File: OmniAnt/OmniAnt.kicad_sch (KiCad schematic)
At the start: 30 parts, among them J1 Conn_01x02_Pin, J2 Conn_01x01, J3 Connector, USB-TYPE-C-16P, J4 Conn_01x01, J5 Conn_01x01, J6 XT30PW-M, J7 XT30PW-M, J8 XT30PW-M, J9 XT30PW-M, U1 ESP32-S3-WROOM-1, U2 TPSM53603RDA, U4 USBLC6-2P6

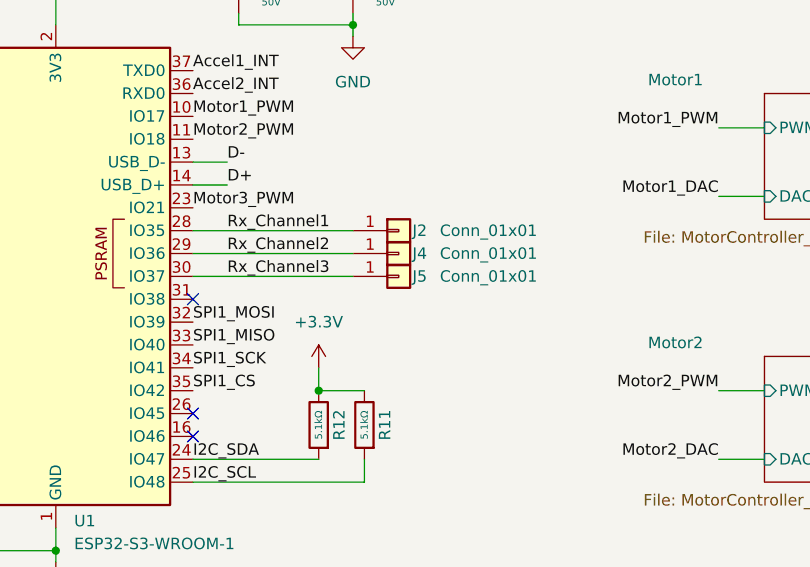
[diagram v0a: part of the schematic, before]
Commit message: added a link to the motor controller datasheet and changed the connector footprint for the RC interface.
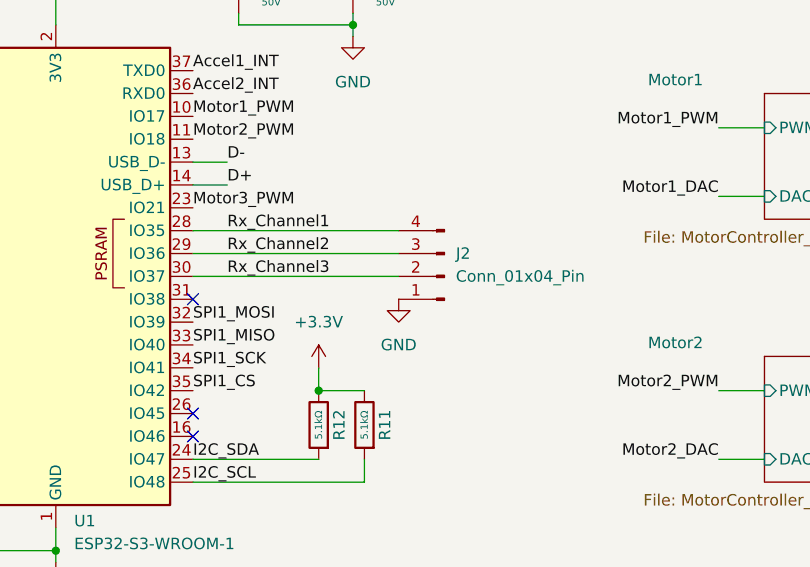
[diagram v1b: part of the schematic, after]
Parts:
- removed J2, J4, J5: Conn_01x01, symbol Connector_Generic:Conn_01x01
- added J2: Conn_01x04_Pin, Connector_PinHeader_2.54mm:PinHeader_1x04_P2.54mm_Vertical, symbol Connector:Conn_01x04_Pin
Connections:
- net GND: now also J2.1 (Pin_1)
- net Rx_Channel1: now also J2.4 (Pin_4)
- net Rx_Channel2: now also J2.3 (Pin_3)
- net Rx_Channel3: now also J2.2 (Pin_2)
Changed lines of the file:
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@@
 	(wire
 		(pts
-			(xy 171.45 127) (xy 189.23 127)
+			(xy 171.45 127) (xy 194.31 127)
 		)
 		(stroke
@@
 	(wire
 		(pts
-			(xy 171.45 124.46) (xy 189.23 124.46)
+			(xy 171.45 124.46) (xy 194.31 124.46)
 		)
 		(stroke
@@
 	(wire
 		(pts
-			(xy 171.45 121.92) (xy 189.23 121.92)
+			(xy 171.45 121.92) (xy 194.31 121.92)
 		)
 		(stroke
@@
 	)
 	(symbol
-		(lib_id "Connector_Generic:Conn_01x01")
-		(at 194.31 124.46 0)
-		(unit 1)
-		(exclude_from_sim no)
-		(in_bom yes)
-		(on_board yes)
-		(dnp no)
-		(property "Reference" "J4"
-			(at 195.834 124.4599 0)
-			(effects
-				(font
-					(size 1.27 1.27)
-				)
-				(justify left)
-			)
-		)
-		(property "Value" "Conn_01x01"
-			(at 198.882 124.46 0)
-			(effects
-				(font
-					(size 1.27 1.27)
-				)
-				(justify left)
-			)
-		)
-		(property "Footprint" ""
-			(at 194.31 124.46 0)
-			(effects
-				(font
-					(size 1.27 1.27)
-				)
-				(hide yes)
-			)
-		)
-		(property "Datasheet" "~"
-			(at 194.31 124.46 0)
-			(effects
-				(font
-					(size 1.27 1.27)
-				)
-				(hide yes)
-			)
-		)
-		(property "Description" "Generic connector, single row, 01x01, script generated (kicad-library-utils/schlib/autogen/connector/)"
-			(at 194.31 124.46 0)
-			(effects
-				(font
-					(size 1.27 1.27)
-				)
-				(hide yes)
-			)
-		)
-		(pin "1"
-		)
-		(instances
-			(project "OmniAnt"
-				(path "/af956454-8f11-4118-89f4-dd7ed925536a"
-					(reference "J4")
-					(unit 1)
-				)
-			)
-		)
-	)
-	(symbol
 		(lib_id "power:GND")
 		(at 115.57 114.3 0)
@@
 	)
 	(symbol
+		(lib_id "power:GND")
+		(at 194.31 129.54 0)
+		(unit 1)
+		(exclude_from_sim no)
+		(in_bom yes)
+		(on_board yes)
+		(dnp no)
+		(fields_autoplaced yes)
+		(property "Reference" "#PWR029"
+			(at 194.31 135.89 0)
+			(effects
+				(font
+					(size 1.27 1.27)
+				)
+				(hide yes)
+			)
+		)
+		(property "Value" "GND"
+			(at 194.31 134.62 0)
+			(effects
+				(font
+					(size 1.27 1.27)
+				)
+			)
+		)
+		(property "Footprint" ""
+			(at 194.31 129.54 0)
+			(effects
+				(font
+					(size 1.27 1.27)
+				)
+				(hide yes)
+			)
+		)
+		(property "Datasheet" ""
+			(at 194.31 129.54 0)
+			(effects
+				(font
+					(size 1.27 1.27)
+				)
+				(hide yes)
+			)
+		)
+		(property "Description" "Power symbol creates a global label with name \"GND\" , ground"
+			(at 194.31 129.54 0)
+			(effects
+				(font
+					(size 1.27 1.27)
+				)
+				(hide yes)
+			)
+		)
+		(pin "1"
+		)
+		(instances
+			(project "OmniAnt"
+				(path "/af956454-8f11-4118-89f4-dd7ed925536a"
+					(reference "#PWR029")
+					(unit 1)
+				)
+			)
+		)
+	)
+	(symbol
 		(lib_id "Power_Protection:USBLC6-2P6")
 		(at 76.2 40.64 0)
@@
 	)
 	(symbol
+		(lib_id "Connector:Conn_01x04_Pin")
+		(at 199.39 127 180)
+		(unit 1)
+		(exclude_from_sim no)
+		(in_bom yes)
+		(on_board yes)
+		(dnp no)
+		(fields_autoplaced yes)
+		(property "Reference" "J2"
+			(at 200.66 124.4599 0)
+			(effects
+				(font
+					(size 1.27 1.27)
+				)
+				(justify right)
+			)
+		)
+		(property "Value" "Conn_01x04_Pin"
+			(at 200.66 126.9999 0)
+			(effects
+				(font
+					(size 1.27 1.27)
+				)
+				(justify right)
+			)
+		)
+		(property "Footprint" "Connector_PinHeader_2.54mm:PinHeader_1x04_P2.54mm_Vertical"
+			(at 199.39 127 0)
+			(effects
+				(font
+					(size 1.27 1.27)
+				)
+				(hide yes)
+			)
+		)
+		(property "Datasheet" "~"
+			(at 199.39 127 0)
+			(effects
+				(font
+					(size 1.27 1.27)
+				)
+				(hide yes)
+			)
+		)
+		(property "Description" "Generic connector, single row, 01x04, script generated"
+			(at 199.39 127 0)
+			(effects
+				(font
+					(size 1.27 1.27)
+				)
+				(hide yes)
+			)
+		)
+		(pin "1"
+		)
+		(pin "3"
+		)
+		(pin "2"
+		)
+		(pin "4"
+		)
+		(instances
+			(project ""
+				(path "/af956454-8f11-4118-89f4-dd7ed925536a"
+					(reference "J2")
+					(unit 1)
+				)
+			)
+		)
+	)
+	(symbol
 		(lib_id "power:GND")
 		(at 62.23 30.48 0)
@@
 	)
 	(symbol
-		(lib_id "Connector_Generic:Conn_01x01")
-		(at 194.31 121.92 0)
-		(unit 1)
-		(exclude_from_sim no)
-		(in_bom yes)
-		(on_board yes)
-		(dnp no)
-		(property "Reference" "J2"
-			(at 195.834 121.9199 0)
-			(effects
-				(font
-					(size 1.27 1.27)
-				)
-				(justify left)
-			)
-		)
-		(property "Value" "Conn_01x01"
-			(at 198.882 121.92 0)
-			(effects
-				(font
-					(size 1.27 1.27)
-				)
-				(justify left)
-			)
-		)
-		(property "Footprint" ""
-			(at 194.31 121.92 0)
-			(effects
-				(font
-					(size 1.27 1.27)
-				)
-				(hide yes)
-			)
-		)
-		(property "Datasheet" "~"
-			(at 194.31 121.92 0)
-			(effects
-				(font
-					(size 1.27 1.27)
-				)
-				(hide yes)
-			)
-		)
-		(property "Description" "Generic connector, single row, 01x01, script generated (kicad-library-utils/schlib/autogen/connector/)"
-			(at 194.31 121.92 0)
-			(effects
-				(font
-					(size 1.27 1.27)
-				)
-				(hide yes)
-			)
-		)
-		(pin "1"
-		)
-		(instances
-			(project ""
-				(path "/af956454-8f11-4118-89f4-dd7ed925536a"
-					(reference "J2")
-					(unit 1)
-				)
-			)
-		)
-	)
-	(symbol
 		(lib_id "XT30PW-M:XT30PW-M")
 		(at 208.28 26.67 0)
@@
 					(unit 1)
 				)
-			)
-		)
-	)
-	(symbol
-		(lib_id "Connector_Generic:Conn_01x01")
-		(at 194.31 127 0)
-		(unit 1)
-		(exclude_from_sim no)
-		(in_bom yes)
-		(on_board yes)
-		(dnp no)
-		(property "Reference" "J5"
-			(at 195.834 126.9999 0)
-			(effects
-				(font
-					(size 1.27 1.27)
-				)
-				(justify left)
-			)
-		)
-		(property "Value" "Conn_01x01"
-			(at 198.882 127 0)
-			(effects
-				(font
-					(size 1.27 1.27)
-				)
-				(justify left)
-			)
-		)
-		(property "Footprint" ""
-			(at 194.31 127 0)
-			(effects
-				(font
-					(size 1.27 1.27)
-				)
-				(hide yes)
-			)
-		)
-		(property "Datasheet" "~"
-			(at 194.31 127 0)
-			(effects
-				(font
-					(size 1.27 1.27)
-				)
-				(hide yes)
-			)
-		)
-		(property "Description" "Generic connector, single row, 01x01, script generated (kicad-library-utils/schlib/autogen/connector/)"
-			(at 194.31 127 0)
-			(effects
-				(font
-					(size 1.27 1.27)
-				)
-				(hide yes)
-			)
-		)
-		(pin "1"
-		)
-		(instances
-			(project "OmniAnt"
-				(path "/af956454-8f11-4118-89f4-dd7ed925536a"
-					(reference "J5")
-					(unit 1)
-				)

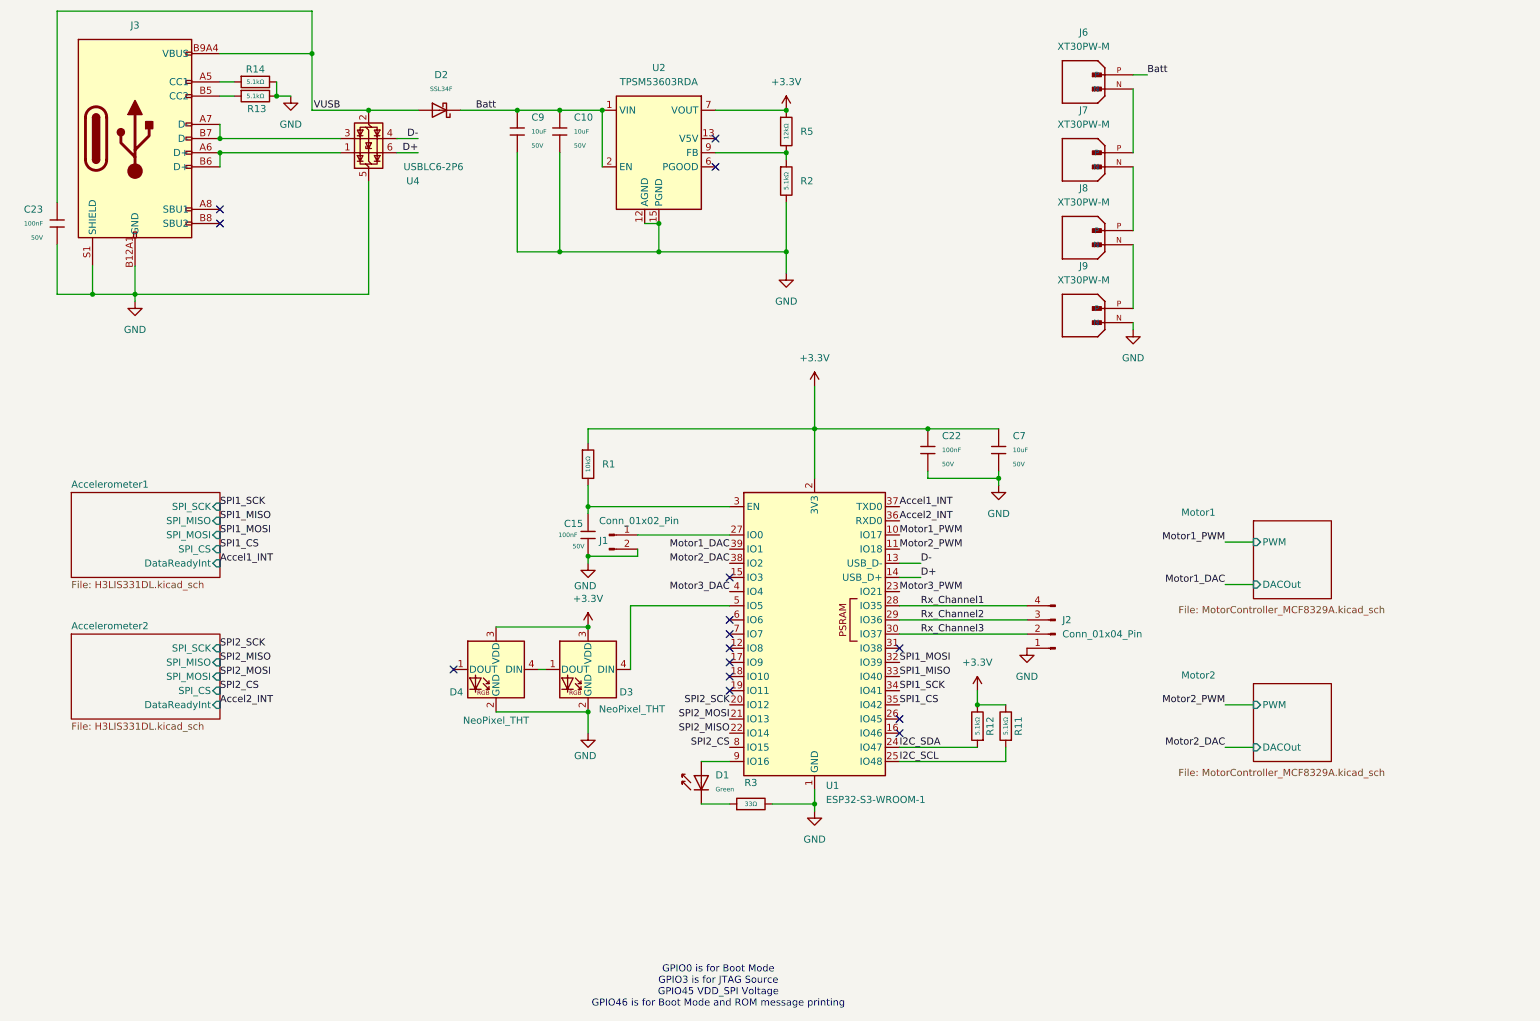
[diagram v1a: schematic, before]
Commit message: fixed all the schematic errors.
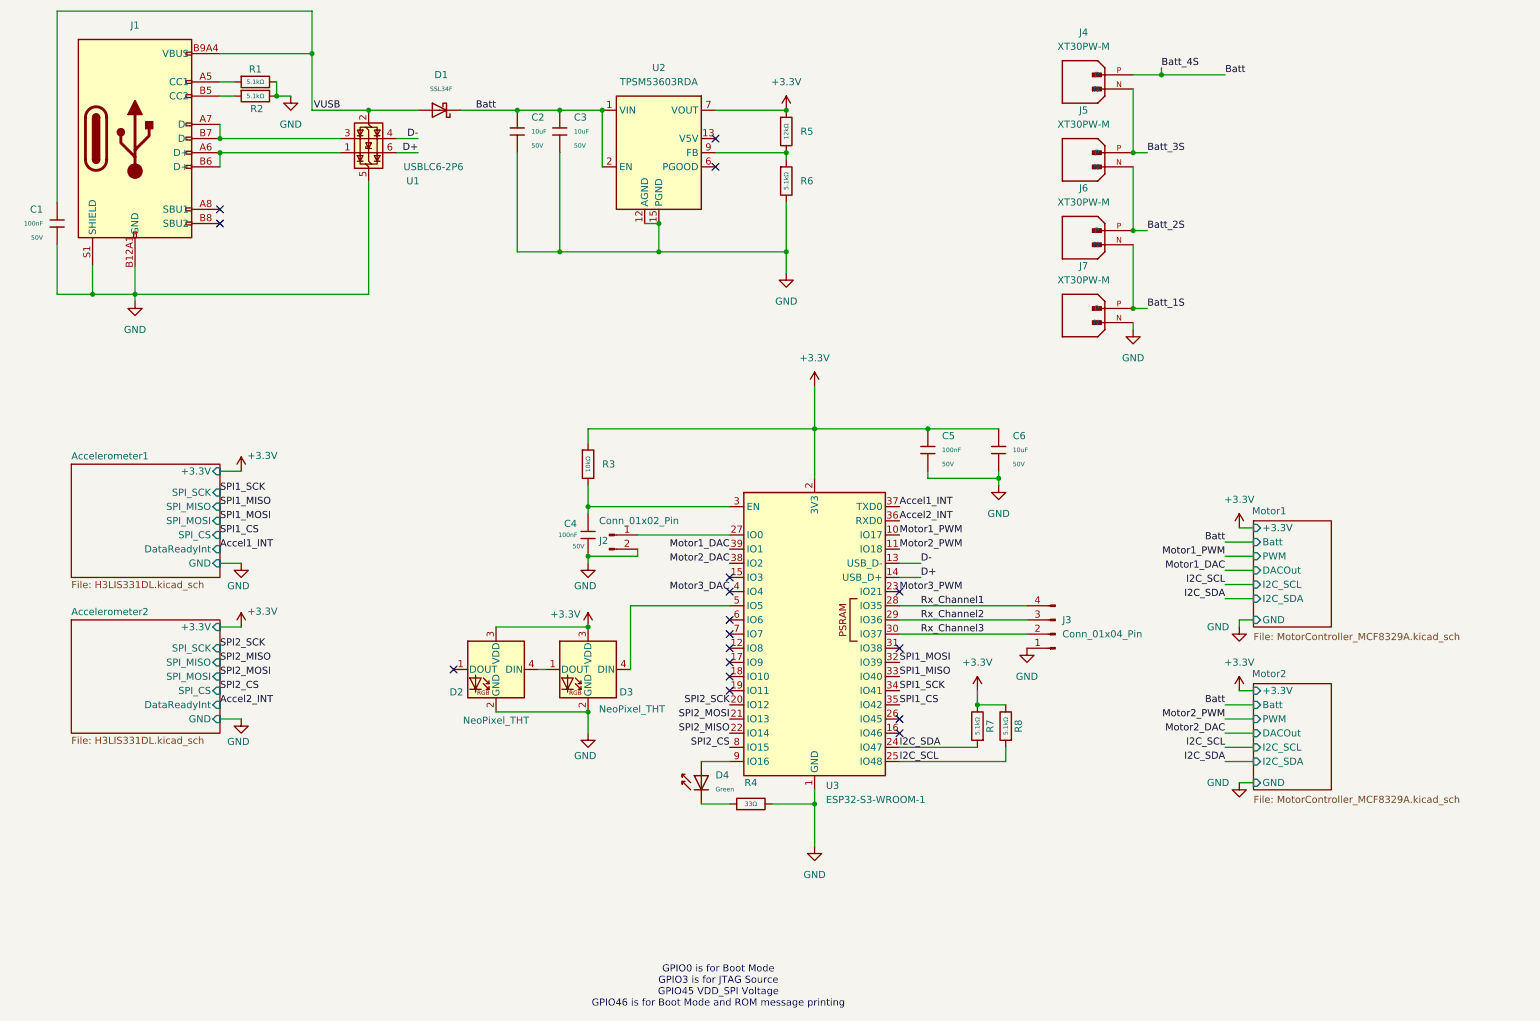
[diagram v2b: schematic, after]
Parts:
- C1: renamed from C23; Stock 64667839 -> 58347526
- C2: renamed from C9; Stock 1647341 -> 1551376
- C3: renamed from C10; Stock 1647341 -> 1551376
- C4: renamed from C15; Stock 64667839 -> 58347526
- C5: renamed from C22; Stock 64667839 -> 58347526
- C6: renamed from C7; Stock 1647341 -> 1551376
- D1: renamed from D2; Stock 1270 -> 1218
- R1: renamed from R14; Stock 4532170 -> 4254023
- R2: renamed from R13; Stock 4532170 -> 4254023
- R3: renamed from R1; Stock 17848646 -> 16030120
- R5: Stock 586700 -> 515895
- R6: renamed from R2; Stock 4532170 -> 4254023
- R7: renamed from R12; Stock 4532170 -> 4254023
- R8: renamed from R11; Stock 4532170 -> 4254023
- renumbered D4 to D2, D1 to D4, J3 to J1, J1 to J2, J2 to J3, J6 to J4, J7 to J5, J8 to J6, J9 to J7, R3 to R4, U4 to U1, U1 to U3
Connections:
- net Batt_1S: now reaches J6.N, J7.P
- net Batt_3S: now reaches J4.N, J5.P
- net Batt_2S: now reaches J5.N, J6.P
- no-connect marks 15 -> 17
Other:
- sheet Accelerometer1 ports: added +3.3V, GND; removed none
- sheet Accelerometer2 ports: added +3.3V, GND; removed none
- sheet Motor1 ports: added +3.3V, Batt, GND, I2C_SCL, I2C_SDA; removed none
- sheet Motor2 ports: added +3.3V, Batt, GND, I2C_SCL, I2C_SDA; removed none

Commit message: Major progress on the motor driver layout. Lots of learning with how to draw traces and pours.
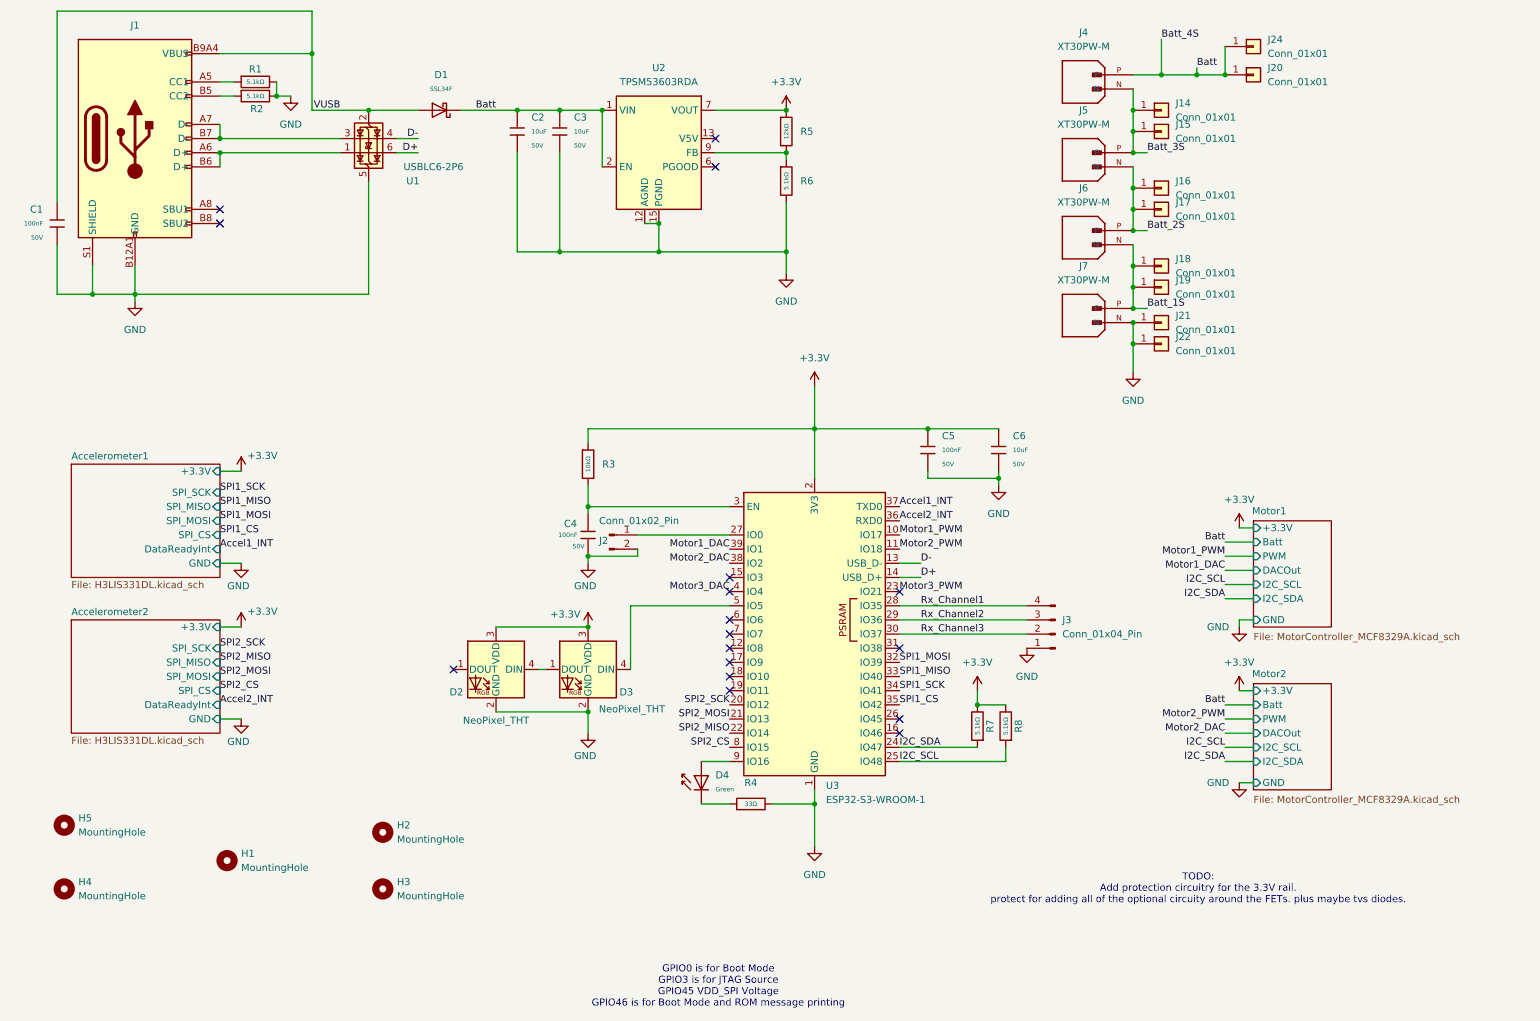
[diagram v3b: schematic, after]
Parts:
- added H1: MountingHole, MountingHole:MountingHole_4.3mm_M4_DIN965, symbol Mechanical:MountingHole
- added H2, H3, H4, H5: MountingHole, MountingHole:MountingHole_3mm, symbol Mechanical:MountingHole
- added J14, J15, J16, J17, J18, J19, J20, J21, J22, J24: Conn_01x01, SolderWire-1.5sqmm_1x01_D1.7mm_OD3mm, symbol Connector_Generic:Conn_01x01
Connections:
- net Batt: now also J20.1 (Pin_1), J24.1 (Pin_1)
- net Batt_1S: now also J18.1 (Pin_1), J19.1 (Pin_1)
- net Batt_2S: now also J16.1 (Pin_1), J17.1 (Pin_1)
- net Batt_3S: now also J14.1 (Pin_1), J15.1 (Pin_1)
- net GND: now also J21.1 (Pin_1), J22.1 (Pin_1)
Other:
- note added: "TODO: Add protection circuitry for the 3.3V rail. protect for adding all of the optional circuity around the FETs. plus maybe tvs diodes."
